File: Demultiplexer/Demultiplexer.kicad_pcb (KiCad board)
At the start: 2 copper layers, 58 parts, among them J101 USB_A, SW101 SW_Push_Dual, SW201 SW_Push_Dual, SW202 SW_Push_Dual, U201 74HC14, U202 74HC74, U301 74HC00, U302 74HC00, U303 74HC00, U304 74HC00, U401 74HC00, U402 74HC00, U403 74HC00, U404 74HC00

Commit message: Working on routing
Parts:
- moved J101 26.5 mm to (204.8, 139.4)
- moved U404 0.73 mm to (203.2, 27.9)
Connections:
- R207 pad 1: /Decoder/~{a_{0}} -> Net-(D203-Pad2)
- R207 pad 2: Net-(D203-Pad2) -> /Decoder/~{a_{0}}
- R208 pad 1: /Decoder/~{a_{1}} -> Net-(D204-Pad2)
- R208 pad 2: Net-(D204-Pad2) -> /Decoder/~{a_{1}}
- U201 pad 12: Net-(U201-Pad12) -> unconnected-(U201-Pad12)
- U201 pad 13: Net-(C204-Pad1) -> GND
- U201 pad 5: unconnected-(U201-Pad5) -> Net-(C204-Pad1)
- U201 pad 6: unconnected-(U201-Pad6) -> Net-(U201-Pad6)
- U202 pad 11: Net-(U201-Pad12) -> Net-(U201-Pad6)
- U401 pad 1: /Output/INPUT -> /Decoder/SELECT0
- U401 pad 2: /Decoder/SELECT0 -> /Output/INPUT
- U402 pad 1: /Output/INPUT -> /Decoder/SELECT1
- U402 pad 2: /Decoder/SELECT1 -> /Output/INPUT
- U403 pad 1: /Output/INPUT -> /Decoder/SELECT2
- U403 pad 2: /Output/SELECT2 -> /Output/INPUT
- U404 pad 1: /Output/INPUT -> /Decoder/SELECT3
- U404 pad 2: /Output/SELECT3 -> /Output/INPUT
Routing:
- net /Decoder/a_{1}: track 0.00 -> 250.5 mm, vias 0 -> 4
- net /Decoder/~{a_{1}}: track 0.00 -> 203.1 mm, vias 0 -> 2
- net /Decoder/a_{0}: track 0.00 -> 193.3 mm
- net /Decoder/~{a_{0}}: track 0.00 -> 168.5 mm, vias 0 -> 1
- net /Output/INPUT: track 0.00 -> 111.6 mm
- net /Decoder/SELECT3: track 0.00 -> 69.1 mm
- net /Decoder/SELECT1: track 0.00 -> 69.1 mm
- net /Decoder/SELECT2: track 0.00 -> 69.1 mm
- net /Decoder/SELECT0: track 0.00 -> 69.1 mm
- net Net-(R202-Pad1): track 0.00 -> 61.1 mm
- net Net-(U201-Pad6): track 0.00 -> 45.5 mm
- net Net-(R201-Pad1): track 0.00 -> 29.7 mm
- net /Input Selectors/~{RESET}: track 0.00 -> 24.7 mm
- net Net-(D203-Pad2): track 0.00 -> 19.9 mm
- net Net-(R401-Pad1): track 0.00 -> 19.9 mm
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- added copper zone on B.Cu, net +5V
- added copper zone on F.Cu, net GND
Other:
- board outline added: 203.2 x 144.8 mm
- board text added: "RGE2022"

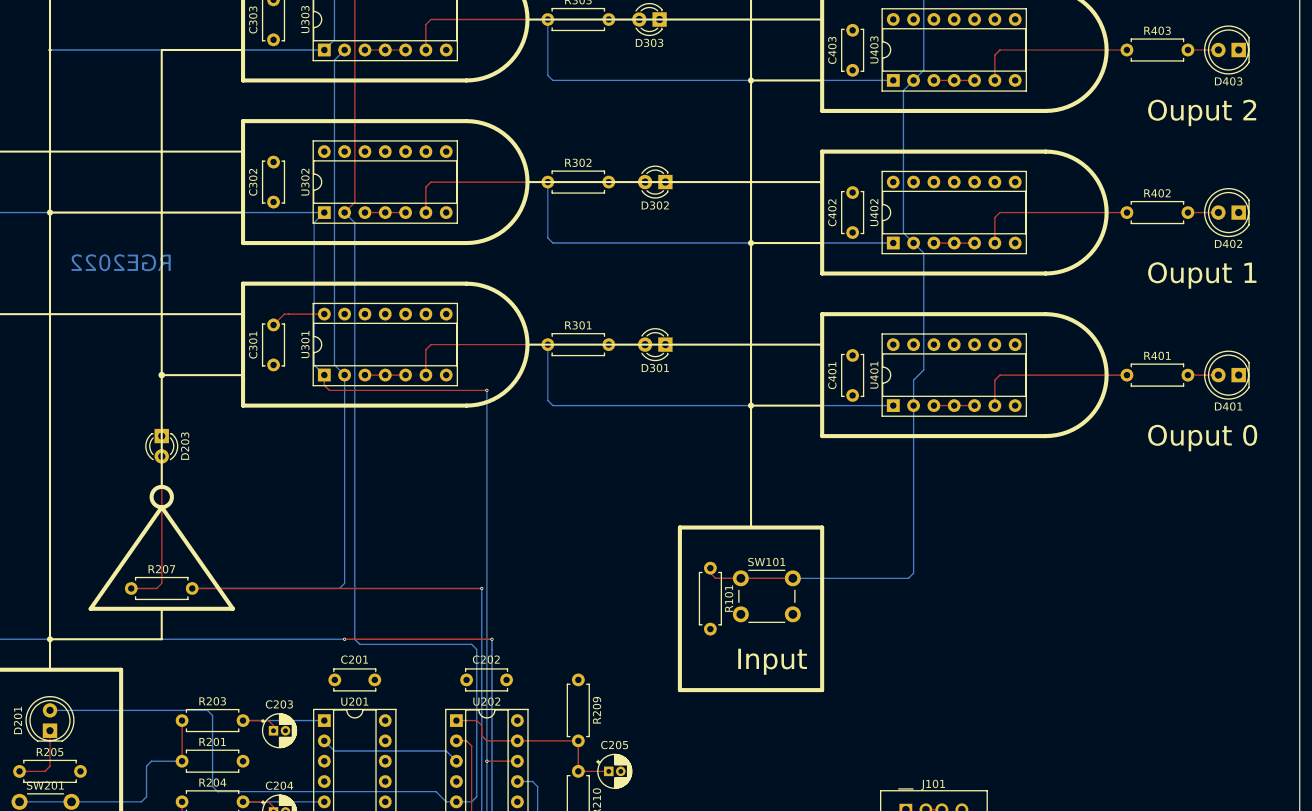
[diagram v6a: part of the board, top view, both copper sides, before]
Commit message: Fixing vias
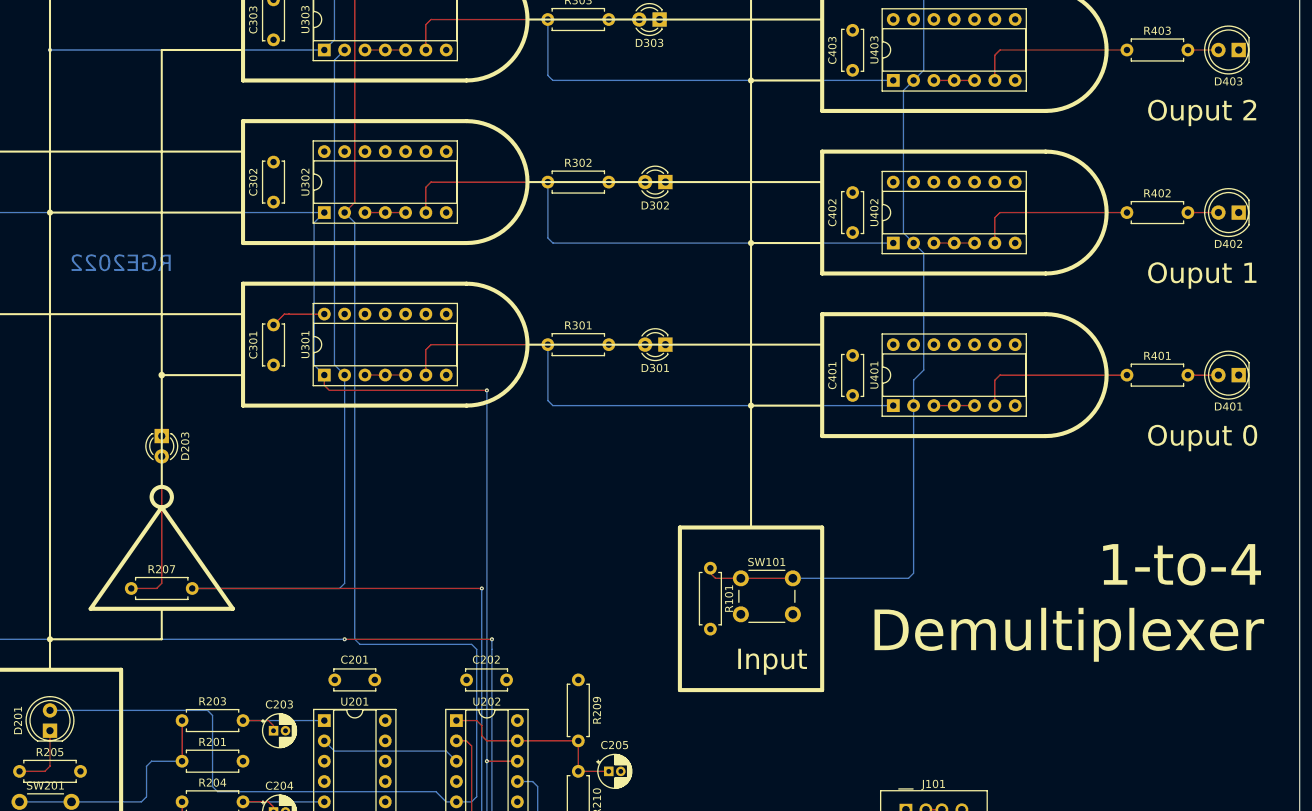
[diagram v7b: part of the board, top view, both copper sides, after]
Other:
- board text added: "1-to-4 Demultiplexer"
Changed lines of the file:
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@@
     (effects (font (size 2.54 2.54) (thickness 0.381)))
+  )
+  (gr_text "1-to-4\nDemultiplexer" (at 249.555 113.03) (layer "F.SilkS")
+    (effects (font (size 5.08 5.08) (thickness 0.6096)) (justify right))
   )
   (gr_text "Ouput 1" (at 248.92 72.39) (layer "F.SilkS")
@@
   (segment (start 132.715 86.995) (end 152.4 86.995) (width 0.127) (layer "F.Cu") (net 28))
   (segment (start 132.08 85.08) (end 132.08 86.36) (width 0.127) (layer "F.Cu") (net 28))
-  (via (at 152.4 86.995) (size 0.4) (drill 0.20066) (layers "F.Cu" "B.Cu") (net 28))
-  (via (at 152.4 133.35) (size 0.4) (drill 0.20066) (layers "F.Cu" "B.Cu") (net 28))
+  (via (at 152.4 86.995) (size 0.499999) (drill 0.20066) (layers "F.Cu" "B.Cu") (net 28))
+  (via (at 152.4 133.35) (size 0.499999) (drill 0.20066) (layers "F.Cu" "B.Cu") (net 28))
   (segment (start 83.185 64.77) (end 82.55 65.405) (width 0.127) (layer "B.Cu") (net 28))
   (segment (start 82.55 65.405) (end 82.55 111.76) (width 0.127) (layer "B.Cu") (net 28))
@@
   (segment (start 149.86 130.81) (end 150.495 131.445) (width 0.127) (layer "F.Cu") (net 29))
   (segment (start 148.59 130.81) (end 149.86 130.81) (width 0.127) (layer "F.Cu") (net 29))
-  (via (at 151.765 111.76) (size 0.4) (drill 0.20066) (layers "F.Cu" "B.Cu") (net 29))
+  (via (at 151.765 111.76) (size 0.499999) (drill 0.20066) (layers "F.Cu" "B.Cu") (net 29))
   (segment (start 133.985 111.76) (end 134.62 111.125) (width 0.127) (layer "B.Cu") (net 29))
   (segment (start 151.13 140.97) (end 148.59 140.97) (width 0.127) (layer "B.Cu") (net 29))
@@
   (segment (start 97.79 118.11) (end 97.79 44.45) (width 0.127) (layer "F.Cu") (net 33))
   (segment (start 134.62 118.11) (end 153.035 118.11) (width 0.127) (layer "F.Cu") (net 33))
-  (via (at 153.035 118.11) (size 0.4) (drill 0.20066) (layers "F.Cu" "B.Cu") (net 33))
-  (via (at 134.62 118.11) (size 0.4) (drill 0.20066) (layers "F.Cu" "B.Cu") (net 33))
-  (via (at 97.79 118.11) (size 0.4) (drill 0.20066) (layers "F.Cu" "B.Cu") (net 33))
-  (via (at 97.79 44.45) (size 0.4) (drill 0.20066) (layers "F.Cu" "B.Cu") (net 33))
+  (via (at 153.035 118.11) (size 0.499999) (drill 0.20066) (layers "F.Cu" "B.Cu") (net 33))
+  (via (at 134.62 118.11) (size 0.499999) (drill 0.20066) (layers "F.Cu" "B.Cu") (net 33))
+  (via (at 97.79 118.11) (size 0.499999) (drill 0.20066) (layers "F.Cu" "B.Cu") (net 33))
+  (via (at 97.79 44.45) (size 0.499999) (drill 0.20066) (layers "F.Cu" "B.Cu") (net 33))
   (segment (start 153.035 140.335) (end 153.035 119.38) (width 0.127) (layer "B.Cu") (net 33))
   (segment (start 97.79 118.11) (end 134.62 118.11) (width 0.127) (layer "B.Cu") (net 33))

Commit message: Getting ready for production
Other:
- board text added: "JLCJLCJLCJLC"
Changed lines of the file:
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@@
       (layerselection 0x00010fc_ffffffff)
       (disableapertmacros false)
-      (usegerberextensions false)
-      (usegerberattributes true)
-      (usegerberadvancedattributes true)
-      (creategerberjobfile true)
+      (usegerberextensions true)
+      (usegerberattributes false)
+      (usegerberadvancedattributes false)
+      (creategerberjobfile false)
       (svguseinch false)
       (svgprecision 6)
@@
       (plotinvisibletext false)
       (sketchpadsonfab false)
-      (subtractmaskfromsilk false)
+      (subtractmaskfromsilk true)
       (outputformat 1)
       (mirror false)
-      (drillshape 1)
+      (drillshape 0)
       (scaleselection 1)
-      (outputdirectory "")
+      (outputdirectory "gerbers")
     )
   )
@@
     (effects (font (size 2.032 2.032) (thickness 0.3048)) (justify mirror))
   )
+  (gr_text "JLCJLCJLCJLC" (at 208.28 149.225) (layer "B.SilkS")
+    (effects (font (size 1 1) (thickness 0.15)) (justify mirror))
+  )
   (gr_text "Ouput 2" (at 248.92 52.07) (layer "F.SilkS")
